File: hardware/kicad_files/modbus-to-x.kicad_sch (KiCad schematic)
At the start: 39 parts, among them IC1 ESP32-WROOM-32D_M113DH2800PH3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, J1 615006138421, J4 M50-3140545R, Q1 DSS4160U-7, Q2 DSS4160U-7, SW1 SW_Wuerth_450301014042, SW4 3983, U1 LM2596S-3.3, U3 MAX3485, Y1 32.768kHz

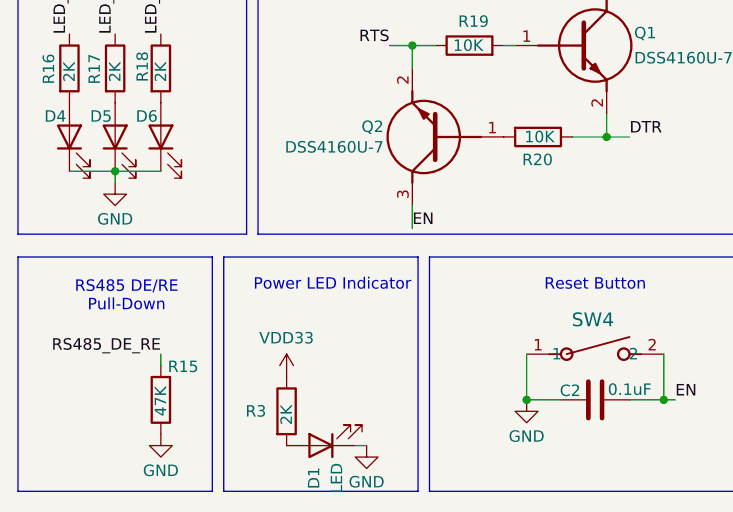
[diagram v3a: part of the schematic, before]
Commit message: updated schema to reflect current configuration model
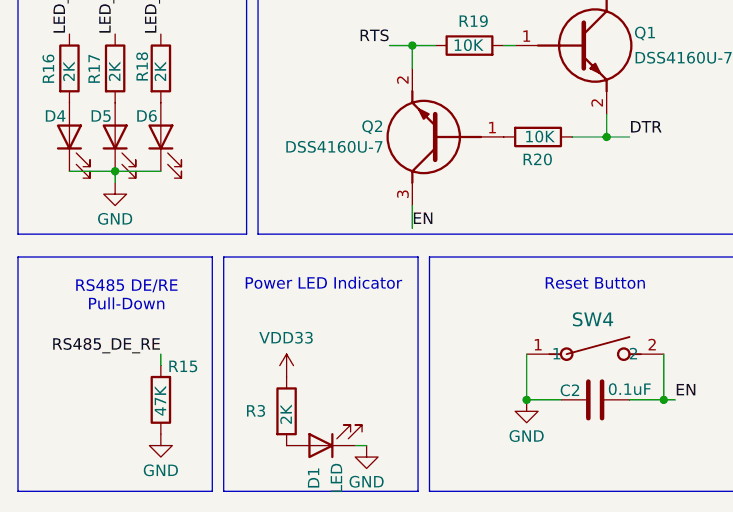
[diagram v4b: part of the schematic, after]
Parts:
- C1, C8: Id C #20 -> (none); InternalId (none) -> C #20
- C22: FriendlyName Cin_MAX3485 -> (none); InternalId (none) -> C #35
- C3, C5: InternalId (none) -> C #8
- C7: footprint Capacitor_SMD:C_1206_3216Metric_Pad1.33x1.80mm_HandSolder -> Capacitor_SMD:C_0805_2012Metric; InternalId (none) -> C #39; PartNo C1206C104K5RACTU -> GCD21BR71H104KA01L
- D3: InternalId (none) -> DIO. #5
- IC1: Height 3.2 -> (none); InternalId (none) -> IC #48; Manufacturer_Name Espressif Systems -> (none); Manufacturer_Part_Number ESP32-WROOM-32D(M113DH2800PH3Q0) -> (none); Mouser Part Number 356-ES32WROOM32D16MB -> (none); Mouser Price/Stock https://www.mouser.co.uk/ProductDetail/Espressif-Systems/ES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 -> (none)
- J1: InternalId (none) -> Conn. #75
- J4: InternalId (none) -> Conn. #28; MANUFACTURER HARWIN -> (none); STANDARD Manufacturer Recommendations -> (none)
- Q1, Q2: Height 1.1 -> (none); InternalId (none) -> TRANS #7; Manufacturer_Name Diodes Incorporated -> (none); Manufacturer_Part_Number DSS4160U-7 -> (none); Mouser Part Number 621-DSS4160U-7 -> (none); Mouser Price/Stock https://www.mouser.co.uk/ProductDetail/Diodes-Incorporated/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 -> (none)
- R14, R2: FriendlyName Rt -> (none); InternalId (none) -> R #13
- U1: InternalId (none) -> IC #43
- U3: InternalId (none) -> IC #36
- Y1: InternalId (none) -> Other #1
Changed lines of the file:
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@@
 	(text "Power LED Indicator"
 		(exclude_from_sim no)
-		(at 49.53 172.72 0)
+		(at 48.514 172.72 0)
 		(effects
 			(font
@@
 			)
 		)
-		(property "Datasheet" ""
+		(property "Datasheet" "https://www.we-online.com/components/products/datasheet/615006138421.pdf"
 			(at 138.43 143.51 0)
 			(effects
@@
 			)
 		)
-		(property "Description" ""
+		(property "Description" "Jack Modular Connector 6p6c (RJ11, RJ12, RJ14, RJ25) 90° Angle (Right) Unshielded Cat5"
 			(at 138.43 143.51 0)
 			(effects
@@
 			)
 		)
+		(property "InternalId" "Conn. #75"
+			(at 138.43 143.51 90)
+			(effects
+				(font
+					(size 1.27 1.27)
+				)
+				(hide yes)
+			)
+		)
 		(pin "3"
 		)
@@
 			)
 		)
+		(property "InternalId" "DIO. #5"
+			(at 147.32 154.94 90)
+			(effects
+				(font
+					(size 1.27 1.27)
+				)
+				(hide yes)
+			)
+		)
 		(pin "2"
 		)
@@
 			)
 		)
-		(property "FriendlyName" "Rt"
-			(at 63.246 108.458 0)
+		(property "PartNo" "RND 1550805S8F6200T5E"
+			(at 60.96 109.22 0)
 			(effects
 				(font
@@
 			)
 		)
-		(property "PartNo" "RND 1550805S8F6200T5E"
+		(property "InternalId" "R #13"
 			(at 60.96 109.22 0)
 			(effects
@@
 			)
 		)
-		(property "FriendlyName" "Rt"
-			(at 63.246 93.218 0)
+		(property "PartNo" "RND 1550805S8F6200T5E"
+			(at 60.96 93.98 0)
 			(effects
 				(font
@@
 			)
 		)
-		(property "PartNo" "RND 1550805S8F6200T5E"
+		(property "InternalId" "R #13"
 			(at 60.96 93.98 0)
 			(effects
@@
 			)
 		)
-		(property "Footprint" "Capacitor_SMD:C_1206_3216Metric_Pad1.33x1.80mm_HandSolder"
+		(property "Footprint" "Capacitor_SMD:C_0805_2012Metric"
 			(at 33.02 89.8652 0)
 			(effects
@@
 			)
 		)
-		(property "Datasheet" "https://content.kemet.com/datasheets/KEM_C1002_X7R_SMD.pdf"
+		(property "Datasheet" "https://search.murata.co.jp/Ceramy/image/img/A01X/G101/ENG/GCJ188R71H104KA12-02B.pdf"
 			(at 36.83 88.9 0)
 			(effects
@@
 			)
 		)
-		(property "Description" "SMD MLC Capacitor 100nF 50V 10% X7R 1206"
+		(property "Description" "0.1 µF ±10% 50V Ceramic Capacitor X7R 0805 (2012 Metric)"
 			(at 36.83 88.9 0)
 			(effects
@@
 			)
 		)
-		(property "PartNo" "C1206C104K5RACTU"
+		(property "PartNo" "GCD21BR71H104KA01L"
 			(at 36.83 88.9 0)
 			(effects
@@
 			)
 		)
+		(property "InternalId" "C #39"
+			(at 36.83 88.9 90)
+			(effects
+				(font
+					(size 1.27 1.27)
+				)
+				(hide yes)
+			)
+		)
 		(pin "2"
 		)
@@
 			)
 		)
+		(property "InternalId" "C #8"
+			(at 110.49 156.21 0)
+			(effects
+				(font
+					(size 1.27 1.27)
+				)
+				(hide yes)
+			)
+		)
 		(pin "2"
 		)
@@
 			)
 		)
-		(property "Height" "3.2"
-			(at 266.7 421.59 0)
-			(effects
-				(font
-					(size 1.27 1.27)
-				)
-				(justify left top)
-				(hide yes)
-			)
-		)
-		(property "Manufacturer_Name" "Espressif Systems"
-			(at 266.7 521.59 0)
-			(effects
-				(font
-					(size 1.27 1.27)
-				)
-				(justify left top)
-				(hide yes)
-			)
-		)
-		(property "Manufacturer_Part_Number" "ESP32-WROOM-32D(M113DH2800PH3Q0)"
-			(at 266.7 621.59 0)
-			(effects
-				(font
-					(size 1.27 1.27)
-				)
-				(justify left top)
-				(hide yes)
-			)
-		)
-		(property "Mouser Part Number" "356-ES32WROOM32D16MB"
-			(at 266.7 721.59 0)
-			(effects
-				(font
-					(size 1.27 1.27)
-				)
-				(justify left top)
-				(hide yes)
-			)
-		)
-		(property "Mouser Price/Stock" "https://www.mouser.co.uk/ProductDetail/Espressif-Systems/ESP32-WROOM-32DM113DH2800PH3Q0?qs=W%2FMpXkg%252BdQ75%2Fda1rSxxJw%3D%3D"
-			(at 266.7 821.59 0)
-			(effects
-				(font
-					(size 1.27 1.27)
-				)
-				(justify left top)
-				(hide yes)
-			)
-		)
-		(property "Arrow Part Number" ""
-			(at 266.7 921.59 0)
-			(effects
-				(font
-					(size 1.27 1.27)
-				)
-				(justify left top)
-				(hide yes)
-			)
-		)
-		(property "Arrow Price/Stock" ""
-			(at 266.7 1021.59 0)
+		(property "PartNo" "M113DH2800PH3Q0"
+			(at 232.41 26.67 0)
 			(effects
 				(font
 					(size 1.27 1.27)
 				)
-				(justify left top)
 				(hide yes)
 			)
 		)
-		(property "PartNo" "M113DH2800PH3Q0"
+		(property "InternalId" "IC #48"
 			(at 232.41 26.67 0)
 			(effects
@@
 			)
 		)
+		(property "InternalId" "IC #36"
+			(at 41.91 106.68 0)
+			(effects
+				(font
+					(size 1.27 1.27)
+				)
+				(hide yes)
+			)
+		)
 		(pin "5"
 		)
@@
 			)
 		)
+		(property "InternalId" "Other #1"
+			(at 110.49 147.32 90)
+			(effects
+				(font
+					(size 1.27 1.27)
+				)
+				(hide yes)
+			)
+		)
 		(pin "1"
 		)
@@
 			)
 		)
-		(property "Id" "C #20"
+		(property "InternalId" "C #20"
 			(at 74.93 41.91 90)
 			(effects
@@
 			)
 		)
-		(property "PARTREV" ""
+		(property "InternalId" "Conn. #28"
 			(at 214.63 151.13 0)
 			(effects
@@
 					(size 1.27 1.27)
 				)
-				(justify bottom)
-				(hide yes)
-			)
-		)
-		(property "MANUFACTURER" "HARWIN"
-			(at 214.63 151.13 0)
-			(effects
-				(font
-					(size 1.27 1.27)
-				)
-				(justify bottom)
-				(hide yes)
-			)
-		)
-		(property "MAXIMUM_PACKAGE_HEIGHT" ""
-			(at 214.63 151.13 0)
-			(effects
-				(font
-					(size 1.27 1.27)
-				)
-				(justify bottom)
-				(hide yes)
-			)
-		)
-		(property "STANDARD" "Manufacturer Recommendations"
-			(at 214.63 151.13 0)
-			(effects
-				(font
-					(size 1.27 1.27)
-				)
-				(justify bottom)
 				(hide yes)
 			)
@@
 			)
 		)
+		(property "InternalId" "C #8"
+			(at 118.11 156.21 0)
+			(effects
+				(font
+					(size 1.27 1.27)
+				)
+				(hide yes)
+			)
+		)
 		(pin "2"
 		)
@@
 			)
 		)
+		(property "InternalId" "IC #43"
+			(at 44.45 38.1 0)
+			(effects
+				(font
+					(size 1.27 1.27)
+				)
+				(hide yes)
+			)
+		)
 		(pin "1"
 		)
@@
 			)
 		)
-		(property "Height" "1.1"
-			(at 54.61 -245.06 0)
-			(effects
-				(font
-					(size 1.27 1.27)
-				)
-				(justify left top)
-				(hide yes)
-			)
-		)
-		(property "Mouser Part Number" "621-DSS4160U-7"
-			(at 54.61 -345.06 0)
-			(effects
-				(font
-					(size 1.27 1.27)
-				)
-				(justify left top)
-				(hide yes)
-			)
-		)
-		(property "Mouser Price/Stock" "https://www.mouser.co.uk/ProductDetail/Diodes-Incorporated/DSS4160U-7?qs=oUsD4qhOtFxSZXssM%2FBZDA%3D%3D"
-			(at 54.61 -445.06 0)
-			(effects
-				(font
-					(size 1.27 1.27)
-				)
-				(justify left top)
-				(hide yes)
-			)
-		)
-		(property "Manufacturer_Name" "Diodes Incorporated"
-			(at 54.61 -545.06 0)
-			(effects
-				(font
-					(size 1.27 1.27)
-				)
-				(justify left top)
-				(hide yes)
-			)
-		)
-		(property "Manufacturer_Part_Number" "DSS4160U-7"
-			(at 54.61 -645.06 0)
+		(property "PartNo" "DSS4160U-7"
+			(at 68.58 156.21 0)
 			(effects
 				(font
 					(size 1.27 1.27)
 				)
-				(justify left top)
 				(hide yes)
 			)
 		)
-		(property "PartNo" "DSS4160U-7"
+		(property "InternalId" "TRANS #7"
 			(at 68.58 156.21 0)
 			(effects
@@
 			)
 		)
-		(property "Id" "C #20"
+		(property "InternalId" "C #20"
 			(at 83.82 41.91 90)
 			(effects
@@
 			)
 		)
-		(property "FriendlyName" "Cin_MAX3485"
-			(at 36.83 83.82 0)
+		(property "InternalId" "C #35"
+			(at 36.83 83.82 90)
 			(effects
 				(font
@@
 			)
 		)
-		(property "Height" "1.1"
-			(at 83.82 547.32 0)
-			(effects
-				(font
-					(size 1.27 1.27)
-				)
-				(justify left top)
-				(hide yes)
-			)
-		)
-		(property "Mouser Part Number" "621-DSS4160U-7"
-			(at 83.82 647.32 0)
-			(effects
-				(font
-					(size 1.27 1.27)
-				)
-				(justify left top)
-				(hide yes)
-			)
-		)
-		(property "Mouser Price/Stock" "https://www.mouser.co.uk/ProductDetail/Diodes-Incorporated/DSS4160U-7?qs=oUsD4qhOtFxSZXssM%2FBZDA%3D%3D"
-			(at 83.82 747.32 0)
-			(effects
-				(font
-					(size 1.27 1.27)
-				)
-				(justify left top)
-				(hide yes)
-			)
-		)
-		(property "Manufacturer_Name" "Diodes Incorporated"
-			(at 83.82 847.32 0)
-			(effects
-				(font
-					(size 1.27 1.27)
-				)
-				(justify left top)
-				(hide yes)
-			)
-		)
-		(property "Manufacturer_Part_Number" "DSS4160U-7"
-			(at 83.82 947.32 0)
+		(property "PartNo" "DSS4160U-7"
+			(at 69.85 146.05 0)
 			(effects
 				(font
 					(size 1.27 1.27)
 				)
-				(justify left top)
 				(hide yes)
 			)
 		)
-		(property "PartNo" "DSS4160U-7"
+		(property "InternalId" "TRANS #7"
 			(at 69.85 146.05 0)
 			(effects

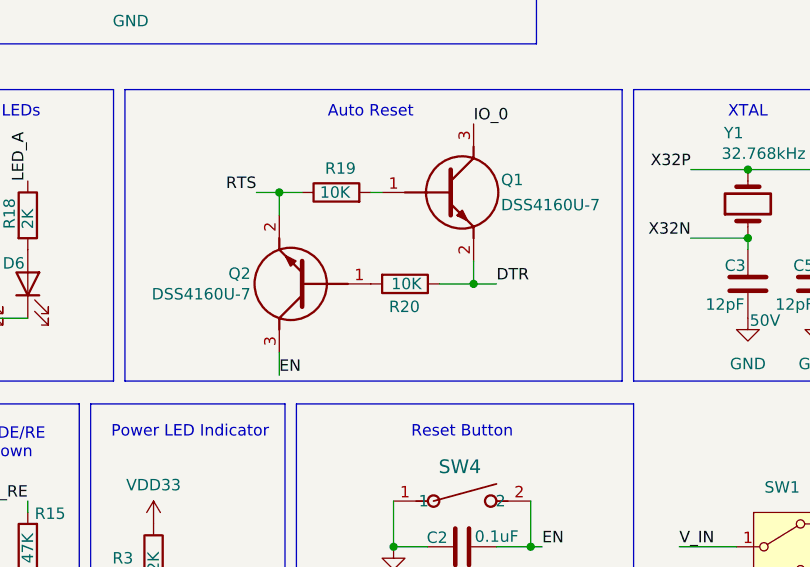
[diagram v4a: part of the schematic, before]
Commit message: added signed OTA changelog
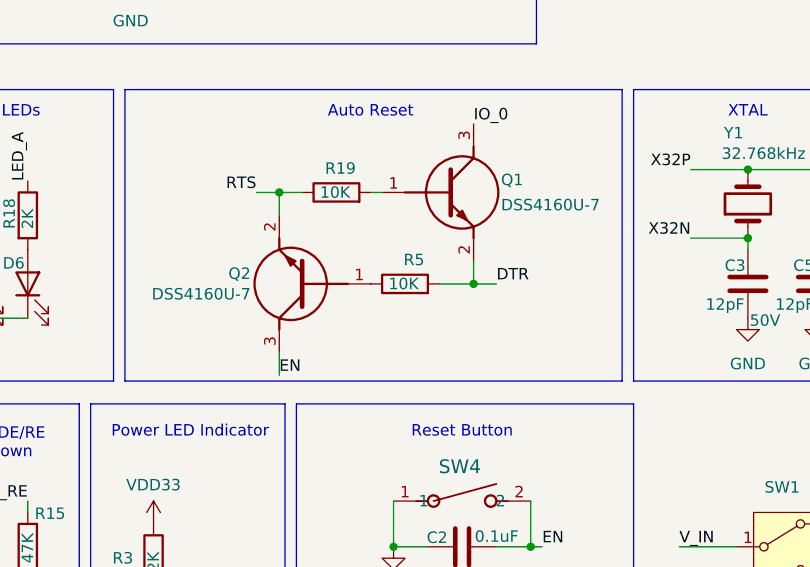
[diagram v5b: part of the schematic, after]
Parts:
- removed R20: 10K, Resistor_SMD:R_0805_2012Metric_Pad1.20x1.40mm_HandSolder, symbol Device:R
- added R5: 10K, Resistor_SMD:R_0603_1608Metric, symbol Device:R
- C2, C24: footprint Capacitor_SMD:C_1206_3216Metric_Pad1.33x1.80mm_HandSolder -> Capacitor_SMD:C_0805_2012Metric; InternalId (none) -> C #39; PartNo C1206C104K5RACTU -> GCD21BR71H104KA01L
- C25: InternalId (none) -> C #17
- C4: InternalId (none) -> C #39; PartNo C1206C104K5RACTU -> GCD21BR71H104KA01L
- C6: InternalId (none) -> C #44
- D1: InternalId (none) -> Reel
- D2: InternalId (none) -> Dio. #10
- D4, D5, D6: InternalId (none) -> REEL
- J4: PartNo M50-3140645R -> M50-3140545R
- L1: InternalId (none) -> IND. #25
- R1: InternalId (none) -> R #32
- R15: InternalId (none) -> R #24
- R16, R17, R18, R3: InternalId (none) -> R #15
- R19, R4: footprint Resistor_SMD:R_0805_2012Metric_Pad1.20x1.40mm_HandSolder -> Resistor_SMD:R_0603_1608Metric; InternalId (none) -> R #35; PartNo RND 155TC0525B1002T5J -> RT0603DRE0710KL
- SW1: InternalId (none) -> Conn. #23
- SW4: InternalId (none) -> Conn. #27; PartNo Adafruit_3983 -> Adafruit-3983
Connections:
- net DTR: now also R5.2
- net at Q2.1 (B): now also R5.1

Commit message: wip
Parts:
- removed D3: SMAJ12A, Diode_SMD:D_SMA_Handsoldering, symbol Diode:SMAJ12A
- removed Y1: 32.768kHz, project_footprints:XTAL_ABS05-32.768KHZ-T, symbol Device:Crystal
- added D7: SS56, Diode_SMD:D_SMA, symbol Device:D_Schottky
- added D8: SMAJ12A, Diode_SMD:D_SMA, symbol Diode:SMAJ12A
- added F1: 2920L150, Fuse:Fuse_2920_7451Metric, symbol Device:Polyfuse_Small
- C3: value 12pF -> 0.1uF; footprint Capacitor_SMD:C_0402_1005Metric_Pad0.74x0.62mm_HandSolder -> Capacitor_SMD:C_0805_2012Metric; Id (none) -> C #43; InternalId C #8 -> (none); PartNo CC0402FRNP09BN120 -> 08055C104KAT2A; Voltage 50V -> (none)
- C5: value 12pF -> 4.7uF; footprint Capacitor_SMD:C_0402_1005Metric_Pad0.74x0.62mm_HandSolder -> Capacitor_SMD:C_0805_2012Metric; InternalId C #8 -> (none); PartNo CC0402FRNP09BN120 -> CL21A475KAQNNNE; Voltage 50V -> 25V
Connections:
- net GND: now also C3.2, C5.2, D8.2 (A2); no longer C3.1, C5.1
- net V_BUCK: now also C3.1, C5.1
- net X32N: no longer C3.2
- net X32P: no longer C5.2
- net V_IN renamed V_PROT
- net V_PROT: now also D7.1 (K), D8.1 (A1); no longer J1.6
- new net: D7.2 (A), F1.1
- new net V_EXT: F1.2, J1.6
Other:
- note added: "Circuit Protection"
- note added: "DE/RE Pull-Down"
- note added: "EXT Connector"
- note removed: "RS485 DE/RE Pull-Down"
- note removed: "XTAL"
- moved on the sheet: C1, C2, C6, C8, D2, L1, SW1, SW4, U1
